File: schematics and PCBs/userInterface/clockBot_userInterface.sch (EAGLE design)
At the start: 6 parts

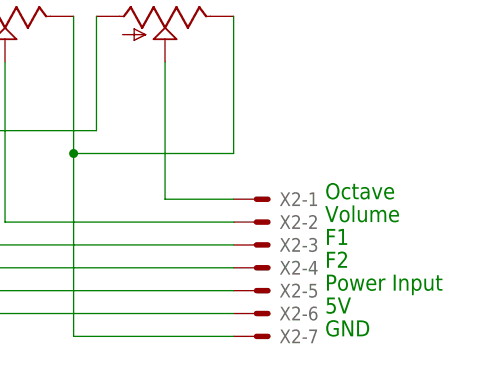
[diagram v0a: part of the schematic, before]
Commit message: Updated user interface
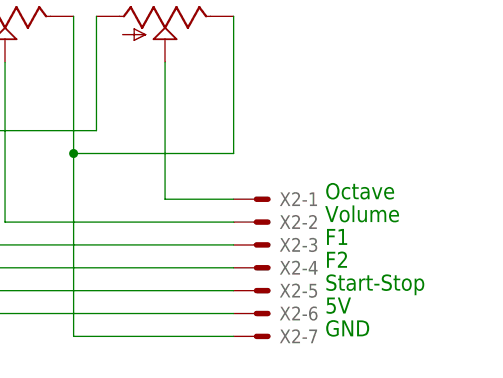
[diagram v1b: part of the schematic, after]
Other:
- note added: "Start-Stop"
- note removed: "Power Input"
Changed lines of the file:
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@@
 <text x="81.28" y="27.94" size="1.778" layer="91">5V</text>
 <text x="81.28" y="25.4" size="1.778" layer="91">GND</text>
-<text x="81.28" y="30.48" size="1.778" layer="91">Power Input</text>
+<text x="81.28" y="30.48" size="1.778" layer="91">Start-Stop</text>
 </plain>
 <instances>

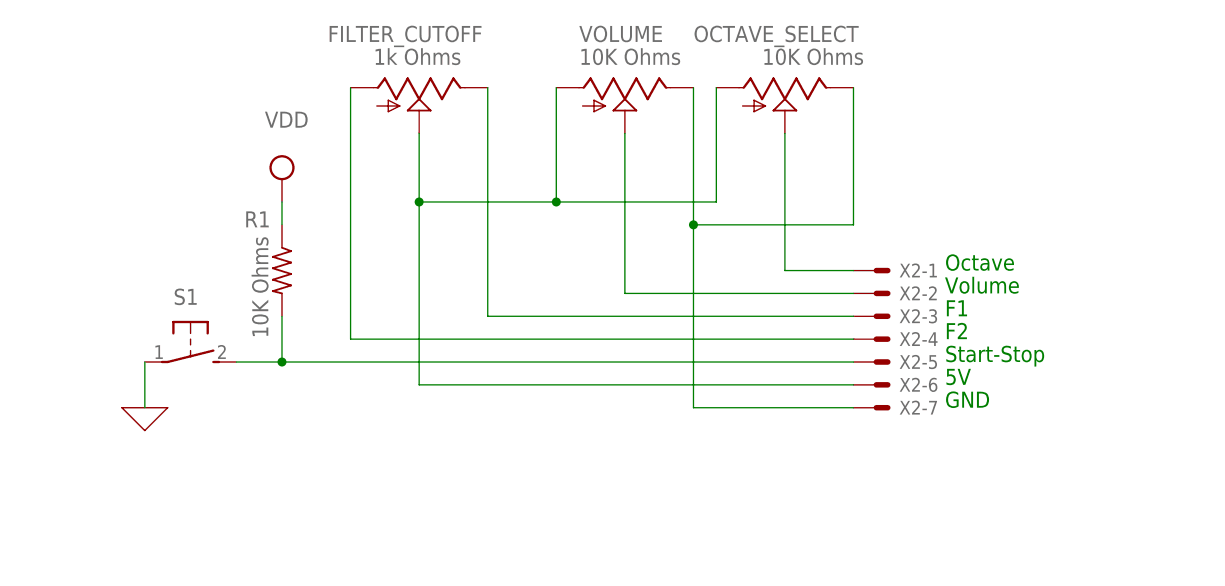
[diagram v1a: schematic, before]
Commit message: 8pin molex user interface
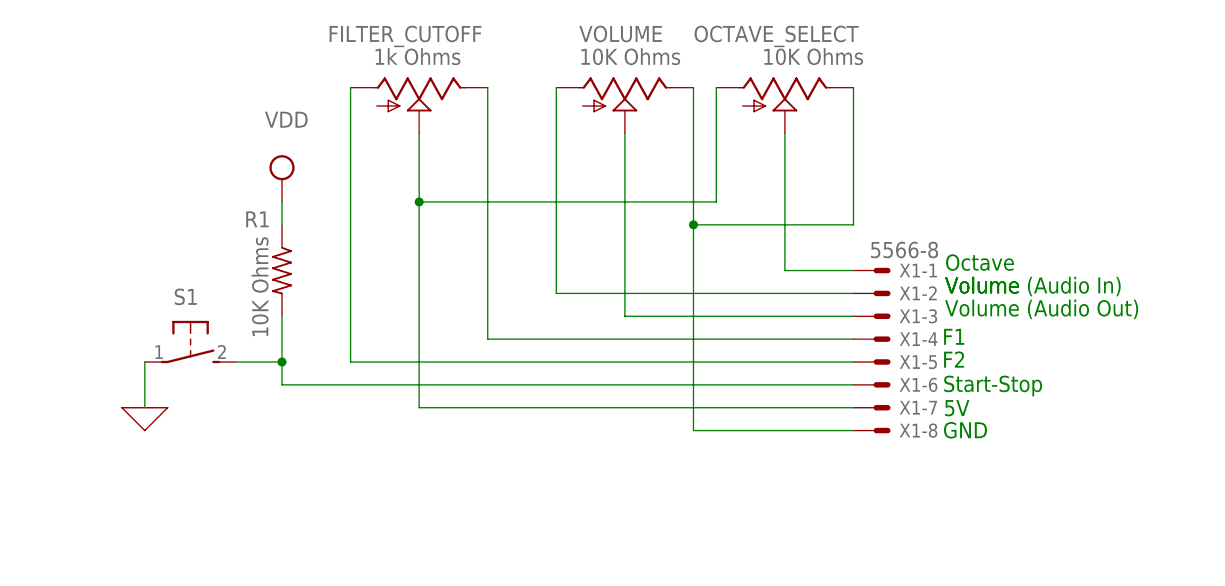
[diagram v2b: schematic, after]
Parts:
- removed X2: (no value), con-molex:KK-156-7
- added X1: 5566-8, con-molex:5566-8
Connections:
- new net N$6: VOLUME.A, X1-2.S
- net N$1: now also X1-6.S; no longer X2-5.S
- net N$10: now also X1-3.S; no longer X2-2.S
- net N$2: now also X1-5.S; no longer X2-4.S
- net N$3: now also X1-4.S; no longer X2-3.S
- net N$4: now also X1-7.S; no longer VOLUME.A, X2-6.S
- net N$5: now also X1-8.S; no longer X2-7.S
- net N$8: now also X1-1.S; no longer X2-1.S
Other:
- note added: "Volume (Audio In)"
- note added: "Volume (Audio Out)"
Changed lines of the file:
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@@
 <part name="X_1" library="ngspice-simulation" library_urn="urn:adsk.eagle:library:527439" deviceset="GND" device=""/>
 <part name="R1" library="adafruit" library_urn="urn:adsk.eagle:library:420" deviceset="FLIPFLOP-RES" device="" package3d_urn="urn:adsk.eagle:package:6240726/1" value="10K Ohms"/>
-<part name="X2" library="con-molex" library_urn="urn:adsk.eagle:library:165" deviceset="KK-156-7" device="" package3d_urn="urn:adsk.eagle:package:8078811/1"/>
+<part name="X1" library="con-molex" library_urn="urn:adsk.eagle:library:165" deviceset="5566-8" device="" package3d_urn="urn:adsk.eagle:package:8078580/1"/>
 </parts>
 <sheets>
@@
 <text x="81.28" y="40.64" size="1.778" layer="91">Octave</text>
 <text x="81.28" y="38.1" size="1.778" layer="91">Volume</text>
-<text x="81.28" y="35.56" size="1.778" layer="91">F1</text>
-<text x="81.28" y="33.02" size="1.778" layer="91">F2</text>
-<text x="81.28" y="27.94" size="1.778" layer="91">5V</text>
-<text x="81.28" y="25.4" size="1.778" layer="91">GND</text>
-<text x="81.28" y="30.48" size="1.778" layer="91">Start-Stop</text>
+<text x="80.9711625" y="32.390646875" size="1.778" layer="91">F1</text>
+<text x="80.9711625" y="29.85065" size="1.778" layer="91">F2</text>
+<text x="81.125584375" y="24.472384375" size="1.778" layer="91">5V</text>
+<text x="81.048375" y="22.009684375" size="1.778" layer="91">GND</text>
+<text x="81.048375" y="27.15604375" size="1.778" layer="91">Start-Stop</text>
+<text x="81.28" y="35.56" size="1.778" layer="91">Volume (Audio Out)</text>
+<text x="81.28" y="38.1" size="1.778" layer="91">Volume (Audio In)</text>
 </plain>
 <instances>
@@
 <attribute name="VALUE" x="4.318" y="44.45" size="1.778" layer="96" rot="R270"/>
 </instance>
-<instance part="X2" gate="-1" x="73.66" y="40.64" smashed="yes">
+<instance part="X1" gate="-1" x="73.66" y="40.64" smashed="yes">
 <attribute name="NAME" x="76.2" y="39.878" size="1.524" layer="95"/>
 <attribute name="VALUE" x="72.898" y="42.037" size="1.778" layer="96"/>
 </instance>
-<instance part="X2" gate="-2" x="73.66" y="38.1" smashed="yes">
+<instance part="X1" gate="-2" x="73.66" y="38.1" smashed="yes">
 <attribute name="NAME" x="76.2" y="37.338" size="1.524" layer="95"/>
 </instance>
-<instance part="X2" gate="-3" x="73.66" y="35.56" smashed="yes">
+<instance part="X1" gate="-3" x="73.66" y="35.56" smashed="yes">
 <attribute name="NAME" x="76.2" y="34.798" size="1.524" layer="95"/>
 </instance>
-<instance part="X2" gate="-4" x="73.66" y="33.02" smashed="yes">
+<instance part="X1" gate="-4" x="73.66" y="33.02" smashed="yes">
 <attribute name="NAME" x="76.2" y="32.258" size="1.524" layer="95"/>
 </instance>
-<instance part="X2" gate="-5" x="73.66" y="30.48" smashed="yes">
+<instance part="X1" gate="-5" x="73.66" y="30.48" smashed="yes">
 <attribute name="NAME" x="76.2" y="29.718" size="1.524" layer="95"/>
 </instance>
-<instance part="X2" gate="-6" x="73.66" y="27.94" smashed="yes">
+<instance part="X1" gate="-6" x="73.66" y="27.94" smashed="yes">
 <attribute name="NAME" x="76.2" y="27.178" size="1.524" layer="95"/>
 </instance>
-<instance part="X2" gate="-7" x="73.66" y="25.4" smashed="yes">
+<instance part="X1" gate="-7" x="73.66" y="25.4" smashed="yes">
 <attribute name="NAME" x="76.2" y="24.638" size="1.524" layer="95"/>
+</instance>
+<instance part="X1" gate="-8" x="73.66" y="22.86" smashed="yes">
+<attribute name="NAME" x="76.2" y="22.098" size="1.524" layer="95"/>
 </instance>
 </instances>
@@
 <segment>
 <pinref part="FILTER_CUTOFF" gate="G$1" pin="E"/>
-<wire x1="30.48" y1="60.96" x2="30.48" y2="35.56" width="0.1524" layer="91"/>
-<wire x1="30.48" y1="35.56" x2="71.12" y2="35.56" width="0.1524" layer="91"/>
-<pinref part="X2" gate="-3" pin="S"/>
+<wire x1="30.48" y1="60.96" x2="30.48" y2="33.02" width="0.1524" layer="91"/>
+<pinref part="X1" gate="-4" pin="S"/>
+<wire x1="30.48" y1="33.02" x2="71.12" y2="33.02" width="0.1524" layer="91"/>
 </segment>
 </net>
@@
 <pinref part="OCTAVE_SELECT" gate="G$1" pin="S"/>
 <wire x1="63.5" y1="55.88" x2="63.5" y2="40.64" width="0.1524" layer="91"/>
-<pinref part="X2" gate="-1" pin="S"/>
+<pinref part="X1" gate="-1" pin="S"/>
 </segment>
 </net>
 <net name="N$10" class="0">
 <segment>
-<wire x1="45.72" y1="38.1" x2="71.12" y2="38.1" width="0.1524" layer="91"/>
 <pinref part="VOLUME" gate="G$1" pin="S"/>
-<wire x1="45.72" y1="55.88" x2="45.72" y2="38.1" width="0.1524" layer="91"/>
-<pinref part="X2" gate="-2" pin="S"/>
+<wire x1="45.72" y1="55.88" x2="45.72" y2="35.56" width="0.1524" layer="91"/>
+<pinref part="X1" gate="-3" pin="S"/>
+<wire x1="45.72" y1="35.56" x2="71.12" y2="35.56" width="0.1524" layer="91"/>
 </segment>
 </net>
@@
 <segment>
 <pinref part="FILTER_CUTOFF" gate="G$1" pin="A"/>
-<wire x1="15.24" y1="60.96" x2="15.24" y2="33.02" width="0.1524" layer="91"/>
-<wire x1="15.24" y1="33.02" x2="71.12" y2="33.02" width="0.1524" layer="91"/>
-<pinref part="X2" gate="-4" pin="S"/>
+<wire x1="15.24" y1="60.96" x2="15.24" y2="30.48" width="0.1524" layer="91"/>
+<pinref part="X1" gate="-5" pin="S"/>
+<wire x1="71.12" y1="30.48" x2="15.24" y2="30.48" width="0.1524" layer="91"/>
 </segment>
 </net>
 <net name="N$4" class="0">
 <segment>
-<pinref part="VOLUME" gate="G$1" pin="A"/>
-<wire x1="22.86" y1="48.26" x2="38.1" y2="48.26" width="0.1524" layer="91"/>
-<wire x1="38.1" y1="48.26" x2="38.1" y2="60.96" width="0.1524" layer="91"/>
 <pinref part="OCTAVE_SELECT" gate="G$1" pin="A"/>
-<wire x1="38.1" y1="48.26" x2="55.88" y2="48.26" width="0.1524" layer="91"/>
+<wire x1="22.86" y1="48.26" x2="55.88" y2="48.26" width="0.1524" layer="91"/>
 <wire x1="55.88" y1="48.26" x2="55.88" y2="60.96" width="0.1524" layer="91"/>
-<junction x="38.1" y="48.26"/>
 <pinref part="FILTER_CUTOFF" gate="G$1" pin="S"/>
 <wire x1="22.86" y1="48.26" x2="22.86" y2="55.88" width="0.1524" layer="91"/>
-<wire x1="22.86" y1="48.26" x2="22.86" y2="27.94" width="0.1524" layer="91"/>
+<wire x1="22.86" y1="48.26" x2="22.86" y2="25.4" width="0.1524" layer="91"/>
 <junction x="22.86" y="48.26"/>
-<pinref part="X2" gate="-6" pin="S"/>
-<wire x1="22.86" y1="27.94" x2="71.12" y2="27.94" width="0.1524" layer="91"/>
+<pinref part="X1" gate="-7" pin="S"/>
+<wire x1="71.12" y1="25.4" x2="22.86" y2="25.4" width="0.1524" layer="91"/>
 </segment>
 </net>
@@
 <pinref part="S1" gate="1" pin="S"/>
 <wire x1="2.54" y1="30.48" x2="7.62" y2="30.48" width="0.1524" layer="91"/>
-<pinref part="X2" gate="-5" pin="S"/>
-<wire x1="7.62" y1="30.48" x2="71.12" y2="30.48" width="0.1524" layer="91"/>
+<pinref part="X1" gate="-6" pin="S"/>
+<wire x1="71.12" y1="27.94" x2="7.62" y2="27.94" width="0.1524" layer="91"/>
+<wire x1="7.62" y1="27.94" x2="7.62" y2="30.48" width="0.1524" layer="91"/>
 <junction x="7.62" y="30.48"/>
 </segment>
@@
 <wire x1="71.12" y1="60.96" x2="71.12" y2="45.72" width="0.1524" layer="91"/>
 <wire x1="53.34" y1="45.72" x2="71.12" y2="45.72" width="0.1524" layer="91"/>
-<wire x1="53.34" y1="45.72" x2="53.34" y2="25.4" width="0.1524" layer="91"/>
+<wire x1="53.34" y1="45.72" x2="53.34" y2="22.86" width="0.1524" layer="91"/>
 <junction x="53.34" y="45.72"/>
-<pinref part="X2" gate="-7" pin="S"/>
-<wire x1="53.34" y1="25.4" x2="71.12" y2="25.4" width="0.1524" layer="91"/>
+<pinref part="X1" gate="-8" pin="S"/>
+<wire x1="53.34" y1="22.86" x2="71.12" y2="22.86" width="0.1524" layer="91"/>
 </segment>
 </net>
@@
 </segment>
 </net>
+<net name="N$6" class="0">
+<segment>
+<pinref part="VOLUME" gate="G$1" pin="A"/>
+<pinref part="X1" gate="-2" pin="S"/>
+<wire x1="38.1" y1="60.96" x2="38.1" y2="38.1" width="0.1524" layer="91"/>
+<wire x1="38.1" y1="38.1" x2="71.12" y2="38.1" width="0.1524" layer="91"/>
+</segment>
+</net>

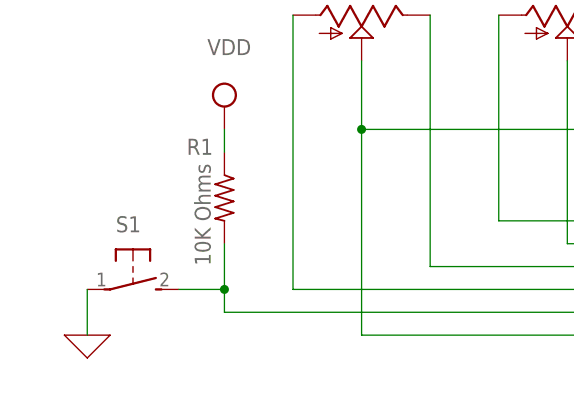
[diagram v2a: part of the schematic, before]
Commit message: Fixed switch on user interface
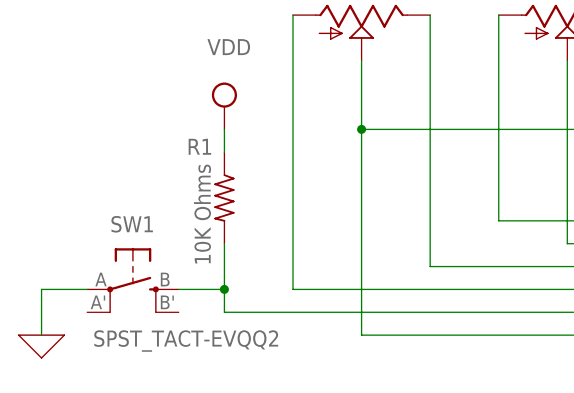
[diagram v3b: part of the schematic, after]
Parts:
- removed S1: (no value), adafruit:31-XX
- added SW1: SPST_TACT-EVQQ2, adafruit:SPST_TACT-EVQQ2
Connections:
- net 0: now also SW1.P; no longer S1.P
- net N$1: now also SW1.S; no longer S1.S
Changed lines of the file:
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@@
 <part name="FILTER_CUTOFF" library="pot" library_urn="urn:adsk.eagle:library:331" deviceset="TRIM_US-" device="S64W" package3d_urn="urn:adsk.eagle:package:22708/1" value="1k Ohms"/>
 <part name="OCTAVE_SELECT" library="pot" library_urn="urn:adsk.eagle:library:331" deviceset="TRIM_US-" device="S64W" package3d_urn="urn:adsk.eagle:package:22708/1" value="10K Ohms"/>
-<part name="S1" library="adafruit" library_urn="urn:adsk.eagle:library:420" deviceset="31-XX" device="" package3d_urn="urn:adsk.eagle:package:6240698/1"/>
 <part name="SUPPLY1" library="supply2" library_urn="urn:adsk.eagle:library:372" deviceset="VDD" device=""/>
 <part name="X_1" library="ngspice-simulation" library_urn="urn:adsk.eagle:library:527439" deviceset="GND" device=""/>
 <part name="R1" library="adafruit" library_urn="urn:adsk.eagle:library:420" deviceset="FLIPFLOP-RES" device="" package3d_urn="urn:adsk.eagle:package:6240726/1" value="10K Ohms"/>
 <part name="X1" library="con-molex" library_urn="urn:adsk.eagle:library:165" deviceset="5566-8" device="" package3d_urn="urn:adsk.eagle:package:8078580/1"/>
+<part name="SW1" library="adafruit" library_urn="urn:adsk.eagle:library:420" deviceset="SPST_TACT" device="-EVQQ2" package3d_urn="urn:adsk.eagle:package:6240643/1"/>
 </parts>
 <sheets>
@@
 <attribute name="VALUE" x="60.96" y="63.5" size="1.778" layer="96"/>
 </instance>
-<instance part="S1" gate="1" x="-2.54" y="30.48" smashed="yes" rot="R270">
-<attribute name="NAME" x="-4.445" y="36.83" size="1.778" layer="95"/>
-<attribute name="VALUE" x="0.635" y="34.29" size="1.778" layer="96"/>
-</instance>
 <instance part="SUPPLY1" gate="G$1" x="7.62" y="50.8" smashed="yes">
 <attribute name="VALUE" x="5.715" y="56.515" size="1.778" layer="96"/>
 </instance>
-<instance part="X_1" gate="G$1" x="-7.62" y="25.4" smashed="yes"/>
+<instance part="X_1" gate="G$1" x="-12.7" y="25.4" smashed="yes"/>
 <instance part="R1" gate="G$1" x="7.62" y="40.64" smashed="yes" rot="R270">
 <attribute name="NAME" x="6.35" y="47.2186" size="1.778" layer="95" rot="R180"/>
@@
 <instance part="X1" gate="-8" x="73.66" y="22.86" smashed="yes">
 <attribute name="NAME" x="76.2" y="22.098" size="1.524" layer="95"/>
+</instance>
+<instance part="SW1" gate="G$1" x="-2.54" y="30.48" smashed="yes" rot="R270">
+<attribute name="NAME" x="-5.08" y="36.83" size="1.778" layer="95"/>
+<attribute name="VALUE" x="-6.985" y="24.13" size="1.778" layer="96"/>
 </instance>
 </instances>
@@
 <pinref part="R1" gate="G$1" pin="2"/>
 <wire x1="7.62" y1="35.56" x2="7.62" y2="30.48" width="0.1524" layer="91"/>
-<pinref part="S1" gate="1" pin="S"/>
 <wire x1="2.54" y1="30.48" x2="7.62" y2="30.48" width="0.1524" layer="91"/>
 <pinref part="X1" gate="-6" pin="S"/>
@@
 <wire x1="7.62" y1="27.94" x2="7.62" y2="30.48" width="0.1524" layer="91"/>
 <junction x="7.62" y="30.48"/>
+<pinref part="SW1" gate="G$1" pin="S"/>
 </segment>
 </net>
@@
 <net name="0" class="0">
 <segment>
-<pinref part="S1" gate="1" pin="P"/>
-<wire x1="-7.62" y1="25.4" x2="-7.62" y2="30.48" width="0.1524" layer="91"/>
+<wire x1="-12.7" y1="25.4" x2="-12.7" y2="30.48" width="0.1524" layer="91"/>
 <pinref part="X_1" gate="G$1" pin="0"/>
+<pinref part="SW1" gate="G$1" pin="P"/>
+<wire x1="-7.62" y1="30.48" x2="-12.7" y2="30.48" width="0.1524" layer="91"/>
 </segment>
 </net>

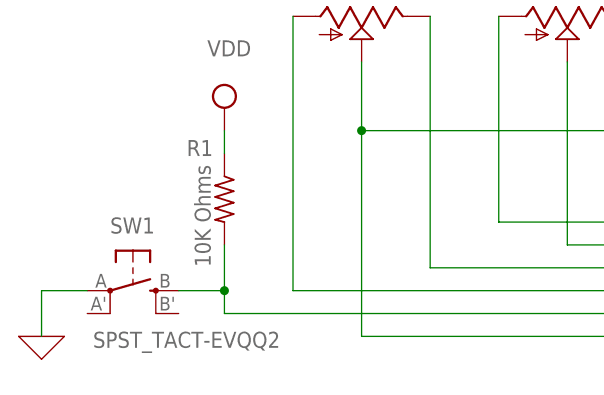
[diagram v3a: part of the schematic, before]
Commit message: User itnerface switch update
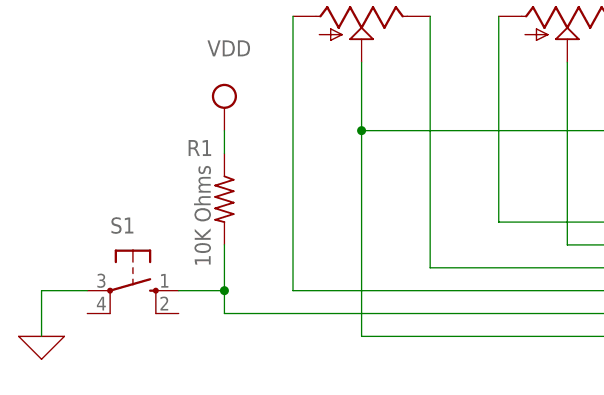
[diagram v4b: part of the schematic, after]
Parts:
- removed SW1: SPST_TACT-EVQQ2, adafruit:SPST_TACT-EVQQ2
- added S1: (no value), switch-omron:10-XX
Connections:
- net 0: now also S1.P; no longer SW1.P
- net N$1: now also S1.S; no longer SW1.S
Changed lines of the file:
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@@
 <part name="R1" library="adafruit" library_urn="urn:adsk.eagle:library:420" deviceset="FLIPFLOP-RES" device="" package3d_urn="urn:adsk.eagle:package:6240726/1" value="10K Ohms"/>
 <part name="X1" library="con-molex" library_urn="urn:adsk.eagle:library:165" deviceset="5566-8" device="" package3d_urn="urn:adsk.eagle:package:8078580/1"/>
-<part name="SW1" library="adafruit" library_urn="urn:adsk.eagle:library:420" deviceset="SPST_TACT" device="-EVQQ2" package3d_urn="urn:adsk.eagle:package:6240643/1"/>
+<part name="S1" library="switch-omron" library_urn="urn:adsk.eagle:library:377" deviceset="10-XX" device="" package3d_urn="urn:adsk.eagle:package:27496/1"/>
 </parts>
 <sheets>
@@
 <attribute name="NAME" x="76.2" y="22.098" size="1.524" layer="95"/>
 </instance>
-<instance part="SW1" gate="G$1" x="-2.54" y="30.48" smashed="yes" rot="R270">
+<instance part="S1" gate="1" x="-2.54" y="30.48" smashed="yes" rot="R270">
 <attribute name="NAME" x="-5.08" y="36.83" size="1.778" layer="95"/>
-<attribute name="VALUE" x="-6.985" y="24.13" size="1.778" layer="96"/>
+<attribute name="VALUE" x="0.635" y="34.29" size="1.778" layer="96"/>
 </instance>
 </instances>
@@
 <wire x1="7.62" y1="27.94" x2="7.62" y2="30.48" width="0.1524" layer="91"/>
 <junction x="7.62" y="30.48"/>
-<pinref part="SW1" gate="G$1" pin="S"/>
+<pinref part="S1" gate="1" pin="S"/>
 </segment>
 </net>
@@
 <wire x1="-12.7" y1="25.4" x2="-12.7" y2="30.48" width="0.1524" layer="91"/>
 <pinref part="X_1" gate="G$1" pin="0"/>
-<pinref part="SW1" gate="G$1" pin="P"/>
 <wire x1="-7.62" y1="30.48" x2="-12.7" y2="30.48" width="0.1524" layer="91"/>
+<pinref part="S1" gate="1" pin="P"/>
 </segment>
 </net>
